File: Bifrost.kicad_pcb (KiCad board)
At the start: 4 copper layers, 68.6 x 53.3 mm, 81 parts, among them J1 OIP, U1 BGA2851, U2 AD5932, U3 LMH6881, U4 BGA2851, U5 AD5932, X1 SPXO-50M

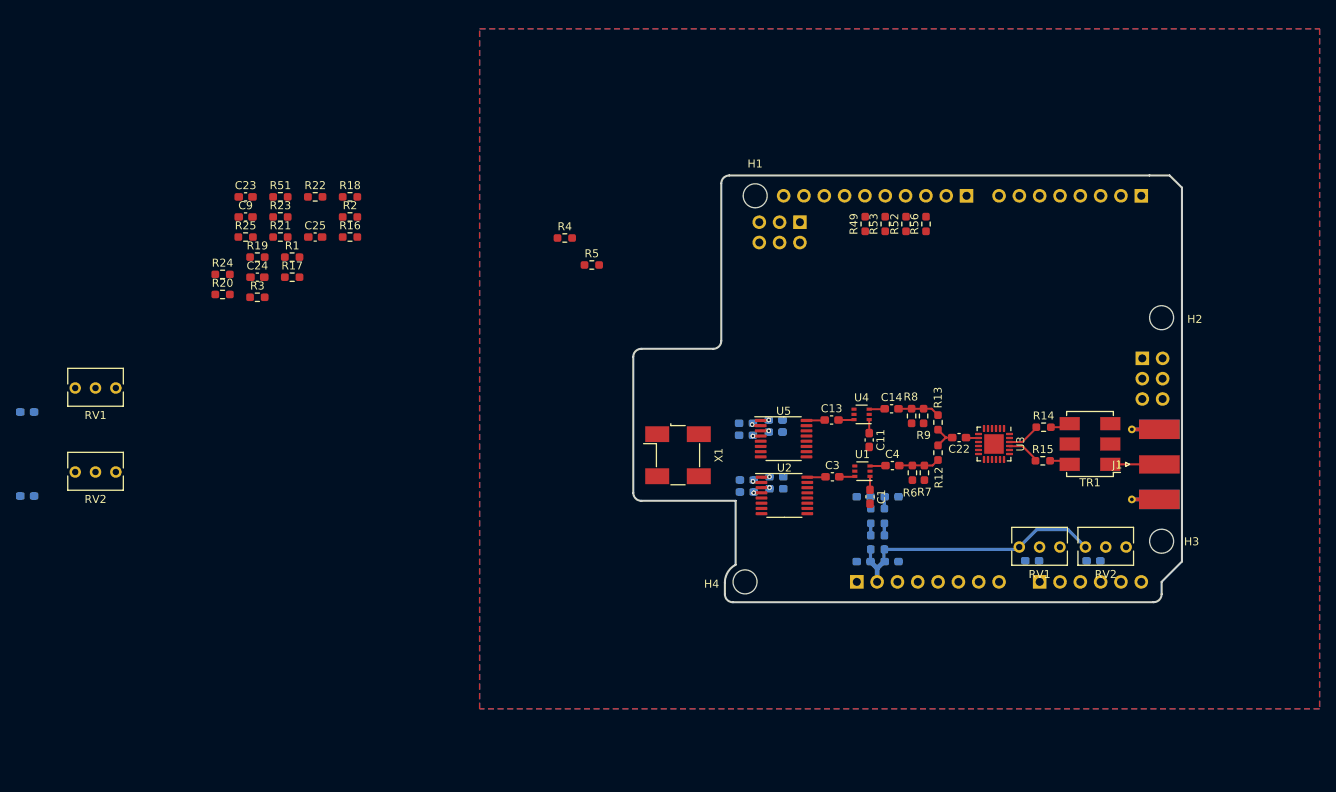
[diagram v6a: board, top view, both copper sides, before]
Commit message: Deleted the fix gain amlifier
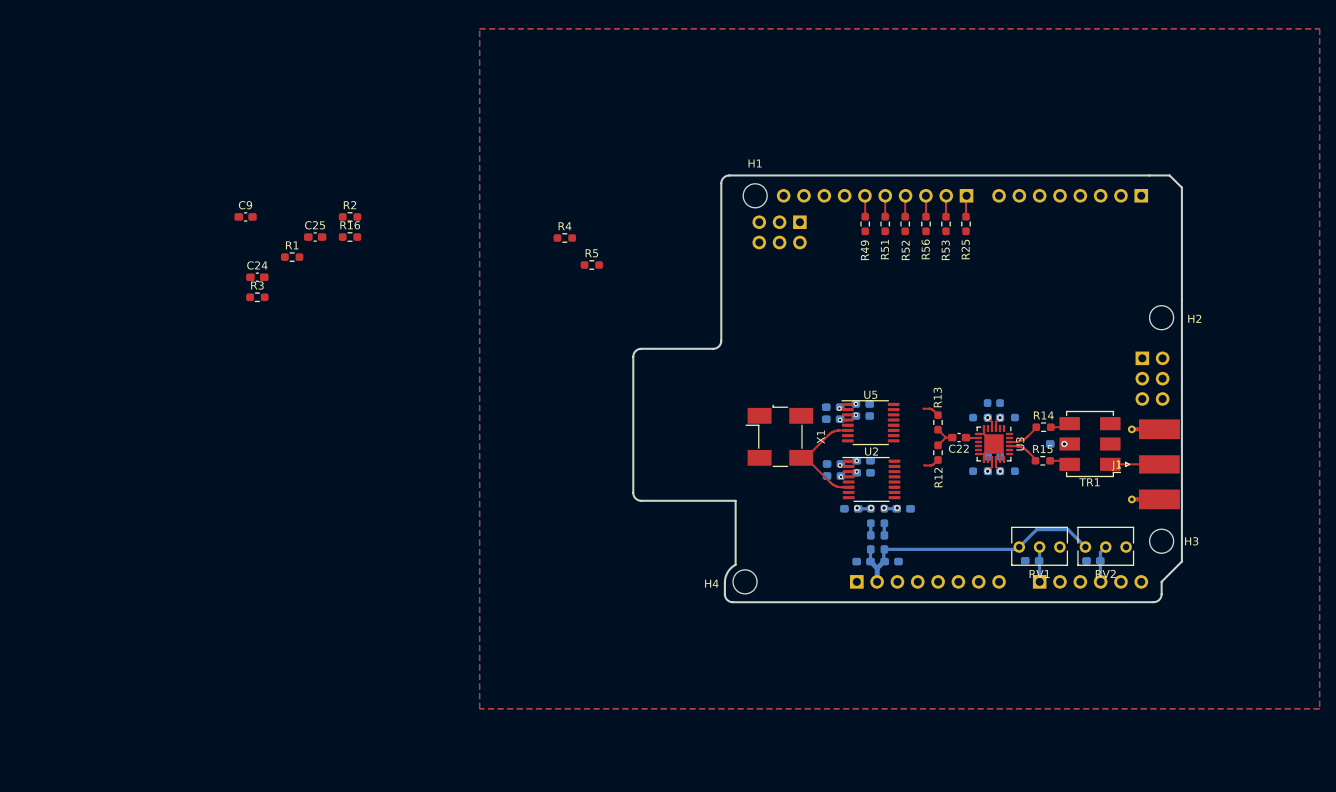
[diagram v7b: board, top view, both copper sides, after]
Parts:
- removed C1, C11: 100n, Capacitor_SMD:C_0603_1608Metric_Pad1.08x0.95mm_HandSolder
- removed C13, C14, C3, C4: 53n, Capacitor_SMD:C_0603_1608Metric_Pad1.08x0.95mm_HandSolder
- removed the C5 at (38.5, 107.9)
- removed the C8 at (38.5, 118.4)
- removed R6, R7, R8, R9: 1k, Resistor_SMD:R_0603_1608Metric_Pad0.98x0.95mm_HandSolder
- removed the RV1 at (44.5, 104.9)
- removed the RV2 at (44.5, 115.4)
- removed U1, U4: BGA2851, Package_TO_SOT_SMD:SOT-363_SC-70-6
- C23, R17, R18, R19, R20, R21, R22, R23, R24: moved to B.Cu
- moved C23 106.0 mm to (167.2, 111.9)
- moved R24 101.2 mm to (161.0, 115.3)
- moved R20 99.3 mm to (161.0, 108.6)
- moved R23 95.1 mm to (160.1, 114.4), turned to 90 degrees
- moved R19 94.8 mm to (160.1, 107.7), turned to 90 degrees
- moved R21 92.9 mm to (158.6, 114.4), turned to 90 degrees
- moved R25 90.1 mm to (155.8, 84.4), turned to 270 degrees
- moved R22 89.9 mm to (157.6, 115.3), turned to 180 degrees
- moved R17 88.5 mm to (158.5, 107.7), turned to 90 degrees
- moved R18 83.5 mm to (157.6, 108.6), turned to 180 degrees
- moved R51 75.7 mm to (145.7, 84.4), turned to 270 degrees
- moved X1 13.0 mm to (132.6, 111.0)
- moved C10 11.1 mm to (139.3, 115.9)
- moved C12 11.1 mm to (142.9, 106.9)
- moved C16 11.1 mm to (142.9, 108.4)
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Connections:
- IOH1 pad 6: /SCK -> /SCLOCK
- R49 pad 1: /SCK -> /SCLOCK
- U2 pad 14: (no net) -> GND
- U2 pad 16: Net-(C3-Pad1) -> /Sheet61C59086/Fout
- U5 pad 14: (no net) -> GND
- U5 pad 16: Net-(C13-Pad1) -> /sheet61E7139B/Fout
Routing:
- net /Sheet61C59086/MCLK: track 0.00 -> 13.4 mm
- net GND: track 0.00 -> 8.53 mm
- net /AD3: track 0.00 -> 4.64 mm
- net /AD0: track 0.00 -> 4.36 mm
- net VCC: track 7.11 -> 3.80 mm, vias 2 -> 4
- net /Sheet61C59086/Fout: track 5.13 -> 1.97 mm
- net /sheet61E7139B/Fout: track 5.27 -> 2.12 mm
- net /IO8: track 0.00 -> 2.64 mm
- net /MOSI: track 0.00 -> 2.63 mm
- net /SCLOCK: track 0.00 -> 2.63 mm
- net /IO9: track 0.00 -> 2.63 mm
- net /SS: track 0.00 -> 2.62 mm
- net /MISO: track 0.00 -> 2.62 mm
- net Net-(C3-Pad1): track 2.30 -> 0.00 mm
- net Net-(C13-Pad1): track 2.30 -> 0.00 mm
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
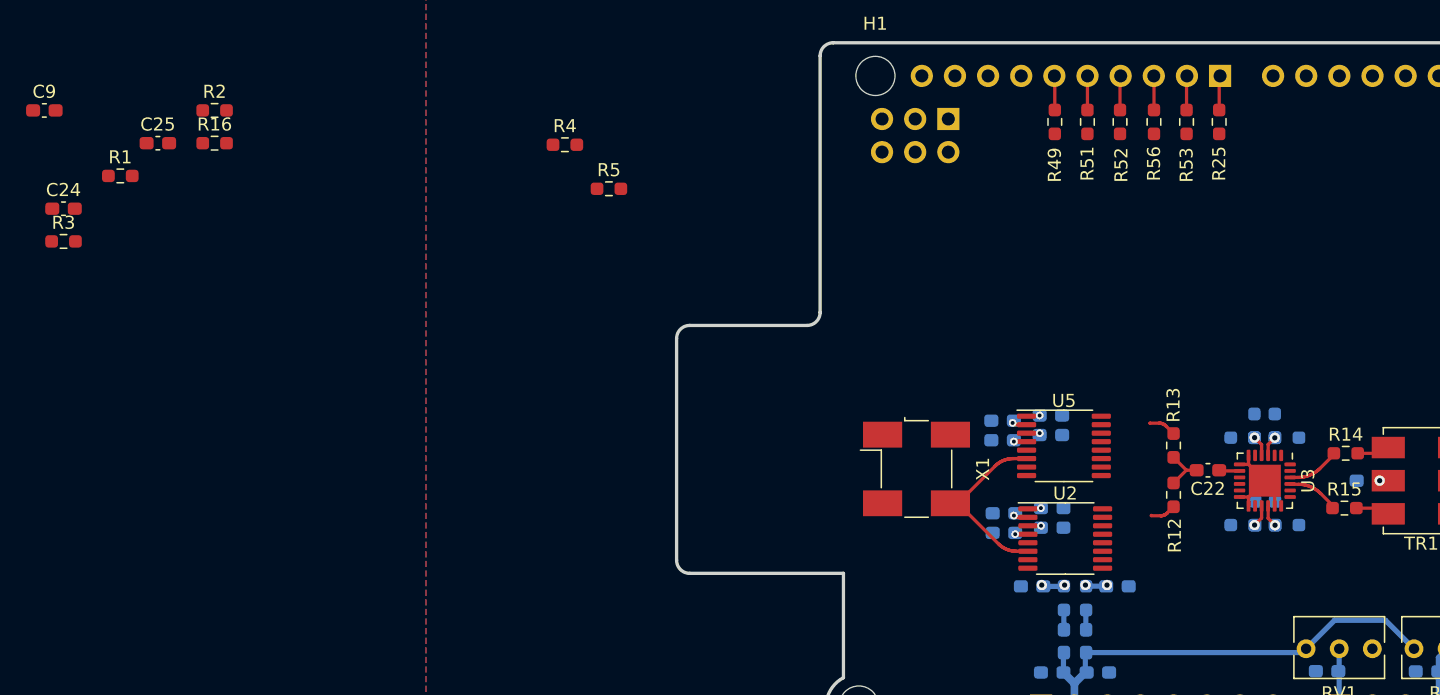
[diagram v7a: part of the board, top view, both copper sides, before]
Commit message: Changed gain pins for the LMH6881 and changed alim for the oscillator
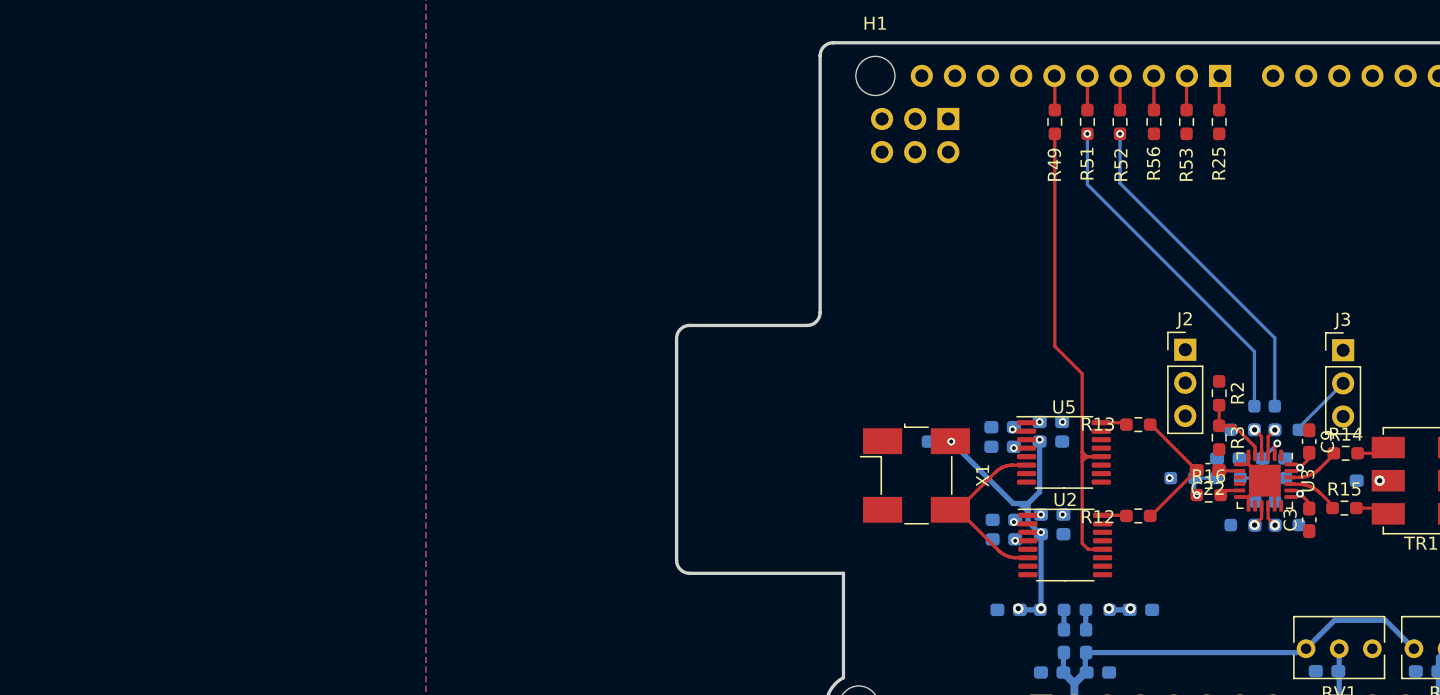
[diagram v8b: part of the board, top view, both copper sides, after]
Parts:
- added C1: 100n, Capacitor_SMD:C_0603_1608Metric_Pad1.08x0.95mm_HandSolder, B.Cu at (134.4, 108.9)
- added C3: 10n, Capacitor_SMD:C_0603_1608Metric_Pad1.08x0.95mm_HandSolder, F.Cu at (162.7, 114.9)
- added J2: Conn_01x03_Male, Connector_PinHeader_2.54mm:PinHeader_1x03_P2.54mm_Vertical, F.Cu at (153.2, 101.9)
- added J3: Conn_01x03_Male, Connector_PinHeader_2.54mm:PinHeader_1x03_P2.54mm_Vertical, F.Cu at (165.3, 101.9)
- C24, C25, R1, R4, R5: moved to B.Cu
- moved C9 100.2 mm to (162.7, 108.9), turned to 270 degrees
- moved C24 91.3 mm to (156.5, 110.2), turned to 180 degrees
- moved R3 89.8 mm to (155.8, 108.6), turned to 270 degrees
- moved C25 88.9 mm to (160.0, 110.2), turned to 180 degrees
- moved R1 88.0 mm to (156.5, 111.7)
- moved R16 80.8 mm to (155.0, 113.0)
- moved R2 80.0 mm to (155.8, 105.2), turned to 270 degrees
- moved R5 55.6 mm to (160.0, 111.7)
- moved R4 53.8 mm to (153.0, 111.7), turned to 180 degrees
- moved R12 3.14 mm to (149.6, 114.6), turned to 0 degrees
- moved R13 3.14 mm to (149.6, 107.6), turned to 0 degrees
- moved C19 2.55 mm to (139.7, 121.8)
- moved C21 2.55 mm to (149.8, 121.8)
- moved R10 1.27 mm to (143.0, 121.8), turned to 0 degrees
- moved R11 1.27 mm to (146.5, 121.8), turned to 180 degrees
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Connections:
- AD1 pad 2: (no net) -> /AD1
- AD1 pad 3: (no net) -> /AD2
- AD1 pad 5: (no net) -> /AD4
- AD1 pad 6: (no net) -> /AD5
- ICSP1 pad 1: (no net) -> /MISO2
- ICSP1 pad 2: (no net) -> /+5V_Adr_3
- ICSP1 pad 3: (no net) -> /SCK2
- ICSP1 pad 4: (no net) -> /MOSI2
- ICSP1 pad 5: (no net) -> /RESET2
- ICSP2 pad 1: (no net) -> /MISO_0
- ICSP2 pad 3: (no net) -> /SCK_0
- ICSP2 pad 4: (no net) -> /MOSI_0
- ICSP2 pad 5: (no net) -> /RESET_0
- IOH1 pad 10: (no net) -> /SCL
- IOH1 pad 8: (no net) -> /AREF
- IOH1 pad 9: (no net) -> /SDA
- IOL1 pad 1: (no net) -> /IO0
- IOL1 pad 2: (no net) -> /IO1
- POWER1 pad 1: (no net) -> Net-(POWER1-Pad1)
- POWER1 pad 3: (no net) -> /RESET
- POWER1 pad 4: (no net) -> /+3V3
- POWER1 pad 5: (no net) -> /+5V_Ard_1
- POWER1 pad 8: (no net) -> /VIN
- R18 pad 2: GND -> Net-(J2-Pad2)
- R20 pad 2: /IO7 -> Net-(J3-Pad2)
- R22 pad 2: /IO4 -> /IO7
- R24 pad 2: GND -> /IO4
- TR1 pad 2: (no net) -> Net-(TR1-Pad2)
- U2 pad 7: (no net) -> Net-(U2-Pad7)
- U2 pad 8: (no net) -> Net-(U2-Pad8)
- U3 pad 10: (no net) -> Net-(U3-Pad10)
- U3 pad 14: Net-(U3-Pad1) -> Net-(U3-Pad14)
- U3 pad 18: Net-(U3-Pad1) -> Net-(U3-Pad18)
- U3 pad 9: (no net) -> Net-(U3-Pad9)
- U5 pad 7: (no net) -> Net-(U5-Pad7)
- U5 pad 8: (no net) -> Net-(U5-Pad8)
- X1 pad 1: (no net) -> Net-(X1-Pad1)
- X1 pad 4: /+5V_Ard_0 -> VDD
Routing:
- net /SCK: track 0.00 -> 37.6 mm
- net /SDO: track 0.00 -> 26.2 mm, vias 0 -> 1
- net /SDI: track 0.00 -> 25.8 mm, vias 0 -> 1
- net VDD: track 3.59 -> 26.0 mm, vias 4 -> 5
- net Net-(C22-Pad2): track 3.58 -> 10.0 mm
- net VCC: track 3.80 -> 10.1 mm, vias 4 -> 9
- net /1.25V: track 0.00 -> 5.81 mm, vias 0 -> 1
- net Net-(R2-Pad2): track 0.00 -> 5.65 mm
- net Net-(J3-Pad2): track 0.00 -> 4.96 mm
- net /2.5V: track 0.00 -> 4.57 mm, vias 0 -> 1
- net Net-(R16-Pad2): track 0.00 -> 1.59 mm
- net Net-(R19-Pad1): track 1.56 -> 2.16 mm
- net Net-(R17-Pad1): track 1.59 -> 2.19 mm
- added copper zone on In2.Cu, net VCC
